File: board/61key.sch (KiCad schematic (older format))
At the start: 142 parts, among them IC1 STM32F042K6T6, SW1 SW_SPST, SW10 SW_SPST, SW11 SW_SPST, SW12 SW_SPST, SW13 SW_SPST, SW14 SW_SPST, SW15 SW_SPST, SW16 SW_SPST, SW17 SW_SPST, SW18 SW_SPST, SW19 SW_SPST, SW2 SW_SPST, SW20 SW_SPST, SW21 SW_SPST, SW22 SW_SPST, SW23 SW_SPST, SW24 SW_SPST, SW25 SW_SPST, SW26 SW_SPST, SW27 SW_SPST, SW28 SW_SPST, SW29 SW_SPST, SW3 SW_SPST, SW30 SW_SPST, SW31 SW_SPST, SW32 SW_SPST, SW33 SW_SPST, SW34 SW_SPST, SW35 SW_SPST, SW36 SW_SPST, SW37 SW_SPST, SW38 SW_SPST, SW39 SW_SPST, SW4 SW_SPST, SW40 SW_SPST, SW41 SW_SPST, SW42 SW_SPST, SW43 SW_SPST, SW44 SW_SPST, SW45 SW_SPST, SW46 SW_SPST, SW47 SW_SPST, SW48 SW_SPST, SW49 SW_SPST, SW5 SW_SPST, SW50 SW_SPST, SW51 SW_SPST, SW52 SW_SPST, SW53 SW_SPST, SW54 SW_SPST, SW55 SW_SPST, SW56 SW_SPST, SW57 SW_SPST, SW58 SW_SPST, SW59 SW_SPST, SW6 SW_SPST, SW60 SW_SPST, SW61 SW_SPST, SW62 SW_SPST, SW63 SW_SPST, SW64 SW_SPST, SW65 SW_SPST, SW66 SW_SPST, SW67 SW_SPST, SW68 SW_SPST, SW69 SW_SPST, SW7 SW_SPST, SW70 SW_SPST, SW71 SW_SPST, SW72 SW_SPST, SW73 SW_SPST, SW74 SW_SPST, SW75 SW_SPST, SW8 SW_SPST, SW9 SW_SPST

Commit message: basic pcb done
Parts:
- added C1, C3, C4: 0.1uF, Capacitor_SMD:C_0603_1608Metric, symbol Device:C
- added C2: 4.7uF, Capacitor_SMD:C_0603_1608Metric, symbol Device:C
- added J1: Conn_ARM_JTAG_SWD_10, Connector_PinHeader_2.54mm:PinHeader_2x05_P2.54mm_Vertical, symbol Connector:Conn_ARM_JTAG_SWD_10
- added R1, R2: 5.1k, Resistor_SMD:R_0603_1608Metric, symbol Device:R_US
- added R3, R4, R5, R6, R7: 1k, Resistor_SMD:R_0603_1608Metric, symbol Device:R_US
- added U1: LD1117S33TR_SOT223, Package_TO_SOT_SMD:SOT-223-3_TabPin2, symbol Regulator_Linear:LD1117S33TR_SOT223
- D1, D10, D11, D12, D13, D14, D15, D16, D17, D18, D19, D2, D20, D21, D22, D23, D24, D25, D26, D27, D28, D29, D3, D30, D31, D32, D33, D34, D35, D36, D37, D38, D39, D4, D40, D41, D42, D43, D44, D45, D46, D47, D48, D49, D5, D50, D51, D52, D53, D54, D55, D56, D57, D58, D59, D6, D60, D61, D62, D63, D64, D65, D7, D8, D9: footprint 61key:D_0805_2012Metric -> Diode_SMD:D_SOD-123F
- IC1: footprint (none) -> 61key:QFP80P900X900X160-32N
- USB1: footprint (none) -> 61key:HRO-TYPE-C-31-M-12
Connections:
- net col0: now also D1.2 (A), D2.2 (A), D3.2 (A), D4.2 (A), D5.2 (A), IC1.8 (PA2); no longer D1.1 (K), D2.1 (K), D3.1 (K), D4.1 (K), D5.1 (K)
- net col1: now also D10.2 (A), D6.2 (A), D63.2 (A), D7.2 (A), D8.2 (A), IC1.9 (PA3); no longer D10.1 (K), D6.1 (K), D63.1 (K), D7.1 (K), D8.1 (K)
- net col10: now also D30.2 (A), D48.2 (A), D49.2 (A), D50.2 (A), D51.2 (A), IC1.27 (PB4); no longer D30.1 (K), D48.1 (K), D49.1 (K), D50.1 (K), D51.1 (K)
- net col11: now also D35.2 (A), D52.2 (A), D53.2 (A), D54.2 (A), D55.2 (A), IC1.28 (PB5); no longer D35.1 (K), D52.1 (K), D53.1 (K), D54.1 (K), D55.1 (K)
- net col12: now also D57.2 (A), D58.2 (A), IC1.29 (PB6); no longer D57.1 (K), D58.1 (K)
- net col13: now also D40.2 (A), D59.2 (A), D60.2 (A), D61.2 (A), D64.2 (A), IC1.30 (PB7); no longer D40.1 (K), D59.1 (K), D60.1 (K), D61.1 (K), D64.1 (K)
- net col14: now also D56.2 (A), D62.2 (A), D65.2 (A), IC1.31 (PB8); no longer D56.1 (K), D62.1 (K), D65.1 (K)
- net col2: now also D11.2 (A), D12.2 (A), D13.2 (A), D15.2 (A), D9.2 (A), IC1.10 (PA4); no longer D11.1 (K), D12.1 (K), D13.1 (K), D15.1 (K), D9.1 (K)
- net col3: now also D14.2 (A), D16.2 (A), D17.2 (A), D18.2 (A), IC1.11 (PA5); no longer D14.1 (K), D16.1 (K), D17.1 (K), D18.1 (K)
- net col4: now also D19.2 (A), D21.2 (A), D22.2 (A), D23.2 (A), IC1.12 (PA6); no longer D19.1 (K), D21.1 (K), D22.1 (K), D23.1 (K)
- net col5: now also D24.2 (A), D26.2 (A), D27.2 (A), D28.2 (A), IC1.13 (PA7); no longer D24.1 (K), D26.1 (K), D27.1 (K), D28.1 (K)
- net col6: now also D20.2 (A), D29.2 (A), D31.2 (A), D32.2 (A), D33.2 (A), IC1.7 (PA1); no longer D20.1 (K), D29.1 (K), D31.1 (K), D32.1 (K), D33.1 (K)
- net col7: now also D34.2 (A), D36.2 (A), D37.2 (A), D38.2 (A), IC1.22 (PA12); no longer D34.1 (K), D36.1 (K), D37.1 (K), D38.1 (K)
- net col8: now also D39.2 (A), D41.2 (A), D42.2 (A), D43.2 (A), IC1.25 (PA15); no longer D39.1 (K), D41.1 (K), D42.1 (K), D43.1 (K)
- net col9: now also D25.2 (A), D44.2 (A), D45.2 (A), D46.2 (A), D47.2 (A), IC1.26 (PB3); no longer D25.1 (K), D44.1 (K), D45.1 (K), D46.1 (K), D47.1 (K)
- net row0: now also R3.1
- net row1: now also R4.1
- net row2: now also R5.1
- net row3: now also SW14.1 (A), SW19.1 (A), SW24.1 (A), SW29.1 (A), SW34.1 (A), SW39.1 (A), SW4.1 (A), SW44.1 (A), SW48.1 (A), SW52.1 (A), SW56.1 (A), SW64.1 (A), SW65.1 (A), SW66.1 (A), SW67.1 (A), SW68.1 (A), SW9.1 (A), R6.1
- net row4: now also R7.1
- net at SW21.2 (B): now also D21.1 (K); no longer D21.2 (A)
- net at SW26.2 (B): now also D26.1 (K); no longer D26.2 (A)
- net at SW31.2 (B): now also D31.1 (K); no longer D31.2 (A)
- net at SW36.2 (B): now also D36.1 (K); no longer D36.2 (A)
- net at SW41.2 (B): now also D41.1 (K); no longer D41.2 (A)
- net at SW45.2 (B): now also D45.1 (K); no longer D45.2 (A)
- net at SW49.2 (B): now also D49.1 (K); no longer D49.2 (A)
- net at SW53.2 (B): now also D53.1 (K); no longer D53.2 (A)
- net at SW16.2 (B): now also D16.1 (K); no longer D16.2 (A)
- net at SW57.2 (B): now also D57.1 (K); no longer D57.2 (A)
- net at SW11.2 (B): now also D11.1 (K); no longer D11.2 (A)
- net at SW6.2 (B): now also D6.1 (K); no longer D6.2 (A)
- net at SW1.2 (B): now also D1.1 (K); no longer D1.2 (A)
- net at SW60.2 (B), SW63.2 (B): now also D60.1 (K); no longer D60.2 (A)
- net at SW59.2 (B), SW74.2 (B): now also D59.1 (K); no longer D59.2 (A)
- net at SW62.2 (B): now also D62.1 (K); no longer D62.2 (A)
- net +3V3: now reaches IC1.1 (VDD)
- net +3V3: now also IC1.17 (VDDIO2), IC1.5 (VDDA), C1.1, C2.1, C3.1, C4.1, J1.1 (VTref), U1.2 (VO)
- net at IC1.14 (PB0): now also R4.2
- net at IC1.15 (PB1): now also R3.2
- net GND: now reaches IC1.16 (VSS)
- net GND: now also IC1.32 (VSSA), USB1.A1 (GND), USB1.A12 (GND), USB1.B1 (GND), USB1.B12 (GND), USB1.S1 (Shell1), USB1.S2 (Shell2), USB1.S3 (Shell3), USB1.S4 (Shell4), C1.2, C2.2, C3.2, C4.2, J1.3 (GND), J1.5 (GND), J1.9 (GNDDetect), R1.1, R2.1, U1.1 (GND)
- net at IC1.18 (PA8): now also R6.2
- net at IC1.19 (PA9): now also R5.2
- net SDA: now reaches IC1.2 (PF0)
- net D+: now reaches IC1.20 (PA10)
- net D+: now also USB1.A6 (D+), USB1.B6 (D+)
- net D-: now reaches IC1.21 (PA11)
- net D-: now also USB1.A7 (D-), USB1.B7 (D-)
- net SWDIO: now reaches IC1.23 (PA13)
- net SWDIO: now also J1.2 (SWDIO/TMS)
- net SWCLK: now reaches IC1.24 (PA14)
- net SWCLK: now also J1.4 (SWDCLK/TCK)
- net SCL: now reaches IC1.3 (PF1)
- net RESET: now reaches IC1.4 (~RST~)
- net RESET: now also J1.10 (~RESET~)
- net at IC1.6 (PA0): now also R7.2
- net at SW61.2 (B), SW75.2 (B): now also D61.1 (K); no longer D61.2 (A)
- net at SW4.2 (B), SW64.2 (B): now also D4.1 (K); no longer D4.2 (A)
- net VBUS: now reaches USB1.A4 (VBUS)
- net VBUS: now also USB1.A9 (VBUS), USB1.B4 (VBUS), USB1.B9 (VBUS), U1.3 (VI)
- net at USB1.A5 (CC1): now also R1.2
- net at USB1.B5 (CC2): now also R2.2
- net at SW65.2 (B): now also D63.1 (K); no longer D63.2 (A)
- net at SW56.2 (B), SW67.2 (B): now also D64.1 (K); no longer D64.2 (A)
- net at SW2.2 (B): now also D2.1 (K); no longer D2.2 (A)
- net at SW12.2 (B): now also D12.1 (K); no longer D12.2 (A)
- net at SW58.2 (B): now also D58.1 (K); no longer D58.2 (A)
- net at SW17.2 (B): now also D17.1 (K); no longer D17.2 (A)
- net at SW54.2 (B): now also D54.1 (K); no longer D54.2 (A)
- net at SW50.2 (B): now also D50.1 (K); no longer D50.2 (A)
- net at SW46.2 (B): now also D46.1 (K); no longer D46.2 (A)
- net at SW42.2 (B): now also D42.1 (K); no longer D42.2 (A)
- net at SW37.2 (B): now also D37.1 (K); no longer D37.2 (A)
- net at SW32.2 (B): now also D32.1 (K); no longer D32.2 (A)
- net at SW27.2 (B): now also D27.1 (K); no longer D27.2 (A)
- net at SW22.2 (B): now also D22.1 (K); no longer D22.2 (A)
- net at SW7.2 (B): now also D7.1 (K); no longer D7.2 (A)
- net at SW3.2 (B): now also D3.1 (K); no longer D3.2 (A)
- net at SW13.2 (B): now also D13.1 (K); no longer D13.2 (A)
- net at SW18.2 (B): now also D18.1 (K); no longer D18.2 (A)
- net at SW55.2 (B): now also D55.1 (K); no longer D55.2 (A)
- net at SW51.2 (B): now also D51.1 (K); no longer D51.2 (A)
- net at SW47.2 (B): now also D47.1 (K); no longer D47.2 (A)
- net at SW43.2 (B): now also D43.1 (K); no longer D43.2 (A)
- net at SW38.2 (B): now also D38.1 (K); no longer D38.2 (A)
- net at SW33.2 (B): now also D33.1 (K); no longer D33.2 (A)
- net at SW28.2 (B): now also D28.1 (K); no longer D28.2 (A)
- net at SW23.2 (B): now also D23.1 (K); no longer D23.2 (A)
- net at SW8.2 (B): now also D8.1 (K); no longer D8.2 (A)
- net at SW14.2 (B): now also D14.1 (K); no longer D14.2 (A)
- net at SW19.2 (B): now also D19.1 (K); no longer D19.2 (A)
- net at SW52.2 (B), SW66.2 (B): now also D52.1 (K); no longer D52.2 (A)
- net at SW48.2 (B): now also D48.1 (K); no longer D48.2 (A)
- net at SW44.2 (B): now also D44.1 (K); no longer D44.2 (A)
- net at SW39.2 (B): now also D39.1 (K); no longer D39.2 (A)
- net at SW34.2 (B): now also D34.1 (K); no longer D34.2 (A)
- net at SW29.2 (B): now also D29.1 (K); no longer D29.2 (A)
- net at SW24.2 (B): now also D24.1 (K); no longer D24.2 (A)
- net at SW9.2 (B): now also D9.1 (K); no longer D9.2 (A)
- net at SW5.2 (B): now also D5.1 (K); no longer D5.2 (A)
- net at SW15.2 (B): now also D15.1 (K); no longer D15.2 (A)
- net at SW20.2 (B): now also D20.1 (K); no longer D20.2 (A)
- net at SW40.2 (B), SW73.2 (B): now also D56.1 (K); no longer D56.2 (A)
- net at SW35.2 (B), SW71.2 (B): now also D35.1 (K); no longer D35.2 (A)
- net at SW30.2 (B), SW70.2 (B): now also D30.1 (K); no longer D30.2 (A)
- net at SW25.2 (B), SW69.2 (B): now also D25.1 (K); no longer D25.2 (A)
- net at SW10.2 (B): now also D10.1 (K); no longer D10.2 (A)
- net at SW72.2 (B): now also D40.1 (K); no longer D40.2 (A)
- net at SW68.2 (B): now also D65.1 (K); no longer D65.2 (A)
- no-connect marks 0 -> 12

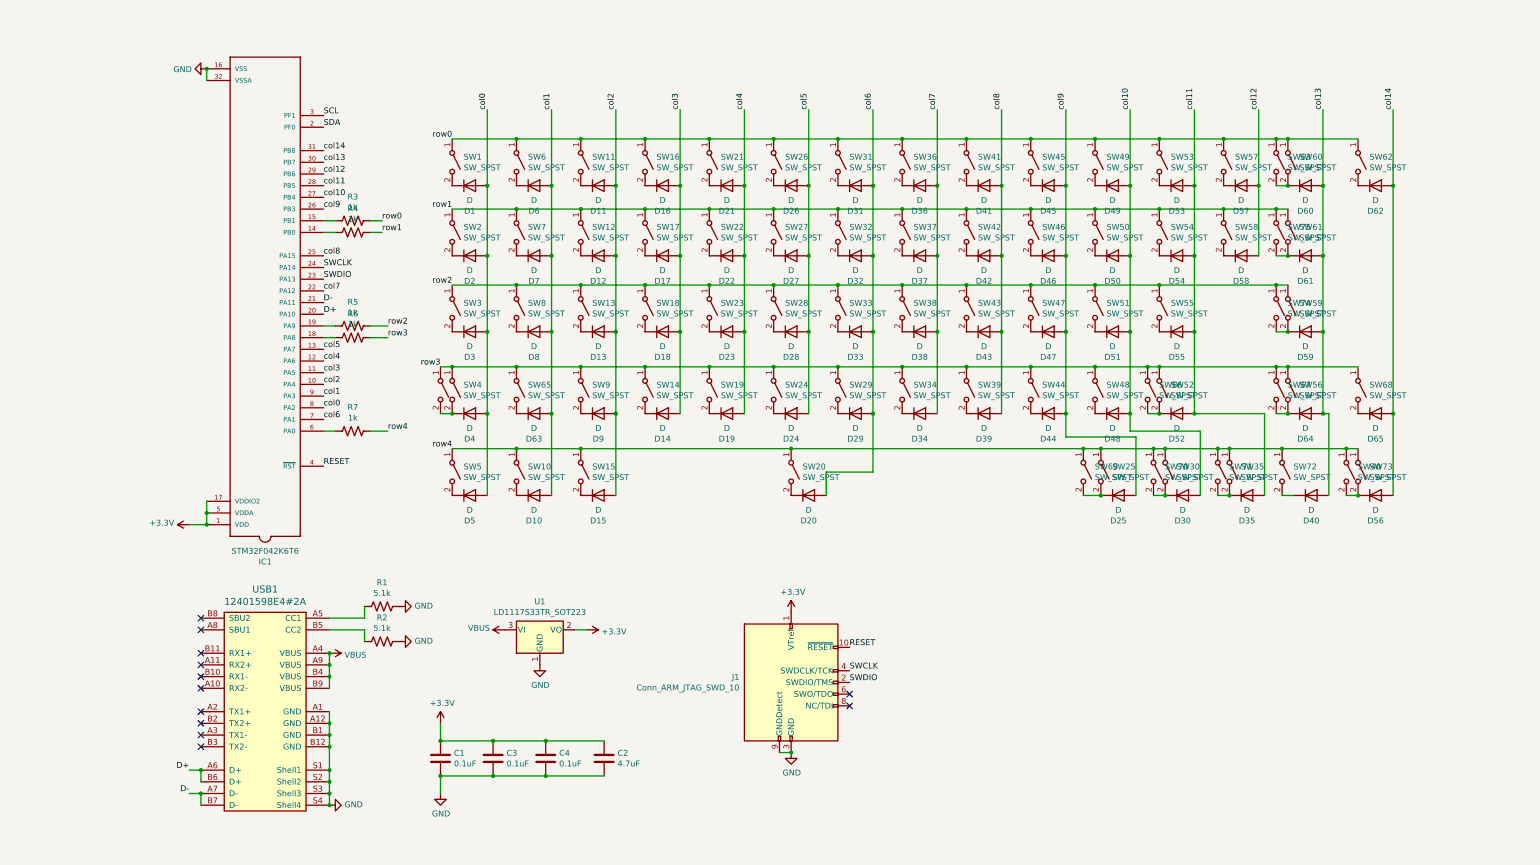
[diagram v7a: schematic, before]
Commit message: need to create models to check board compatibility; prototype candidate
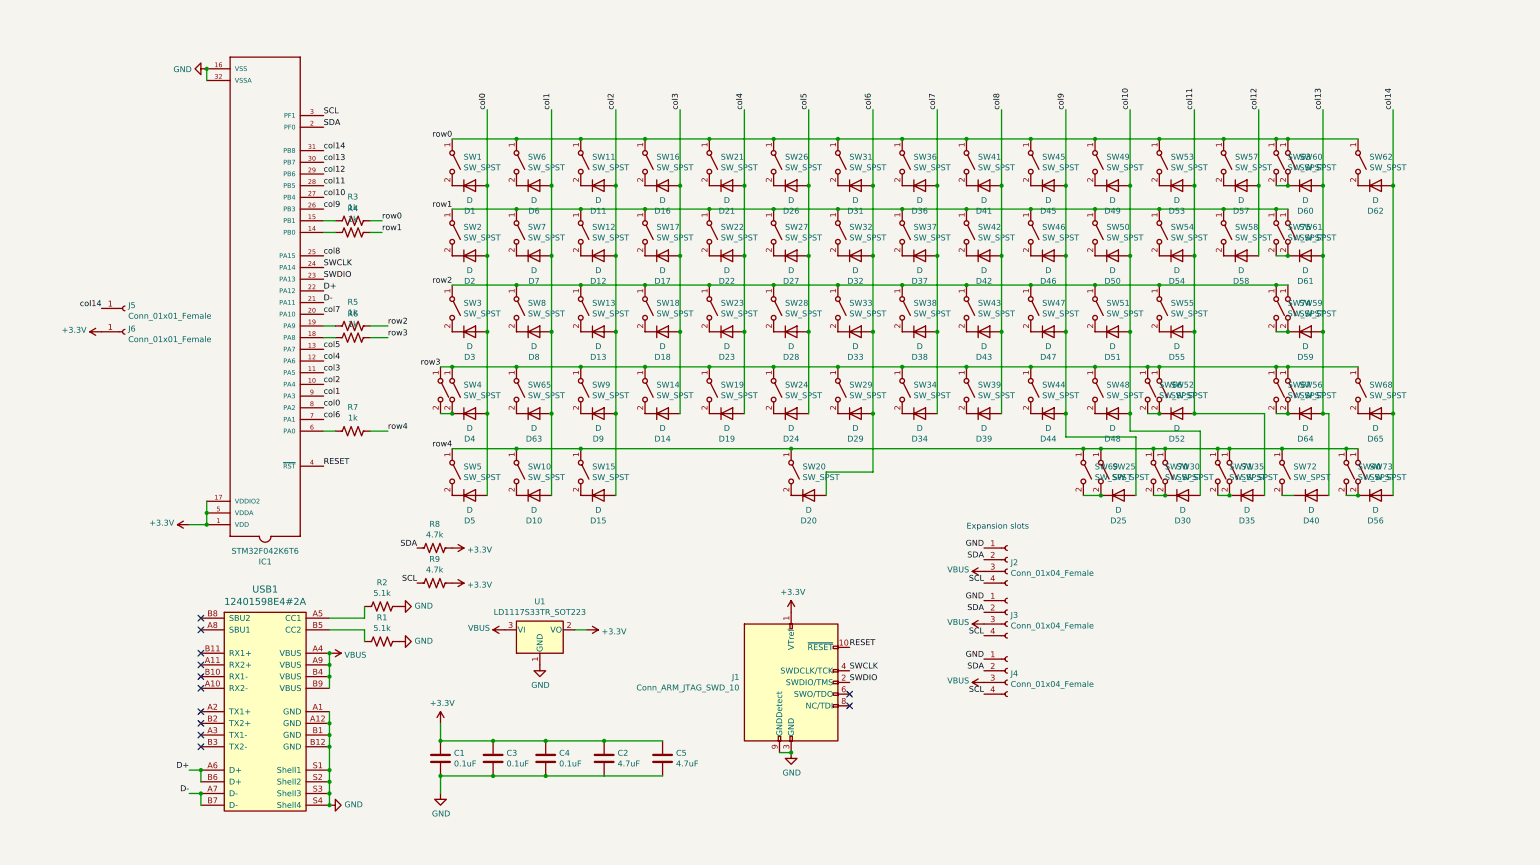
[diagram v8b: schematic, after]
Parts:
- added C5: 4.7uF, Capacitor_SMD:C_0603_1608Metric, symbol Device:C
- added J2, J3, J4: Conn_01x04_Female, 61key:exp_header, symbol Connector:Conn_01x04_Female
- added J5, J6: Conn_01x01_Female, TestPoint:TestPoint_Pad_4.0x4.0mm, symbol Connector:Conn_01x01_Female
- added R8, R9: 4.7k, Resistor_SMD:R_0603_1608Metric, symbol Device:R_US
- D1, D10, D11, D12, D13, D14, D15, D16, D17, D18, D19, D2, D20, D21, D22, D23, D24, D25, D26, D27, D28, D29, D3, D30, D31, D32, D33, D34, D35, D36, D37, D38, D39, D4, D40, D41, D42, D43, D44, D45, D46, D47, D48, D49, D5, D50, D51, D52, D53, D54, D55, D56, D57, D58, D59, D6, D60, D61, D62, D63, D64, D65, D7, D8, D9: footprint Diode_SMD:D_SOD-123F -> 61key:D_SOD-123F
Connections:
- net +3V3: now also C5.1, J6.1 (Pin_1), R8.1, R9.1
- net D+: now also IC1.22 (PA12); no longer IC1.20 (PA10)
- net GND: now also C5.2, J2.1 (Pin_1), J3.1 (Pin_1), J4.1 (Pin_1)
- net SCL: now also J2.4 (Pin_4), J3.4 (Pin_4), J4.4 (Pin_4), R9.2
- net SDA: now also J2.2 (Pin_2), J3.2 (Pin_2), J4.2 (Pin_2), R8.2
- net VBUS: now also J2.3 (Pin_3), J3.3 (Pin_3), J4.3 (Pin_3)
- net col14: now also J5.1 (Pin_1)
- net col7: now also IC1.20 (PA10); no longer IC1.22 (PA12)
- net at USB1.A5 (CC1): now also R2.2; no longer R1.2
- net at USB1.B5 (CC2): now also R1.2; no longer R2.2
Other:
- note added: "Expansion slots"
- moved on the sheet: R1, R2
